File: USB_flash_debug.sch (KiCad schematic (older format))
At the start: 31 parts, among them IC2 TPS7A0518PDBVT, J6 E8124-015-01, J9 E8124-015-01, Q7 BSS138-7-F, Q8 BSS138-7-F, SW1 1X03, U13 FT232RQ-REEL, U9 FSUSB30MUX

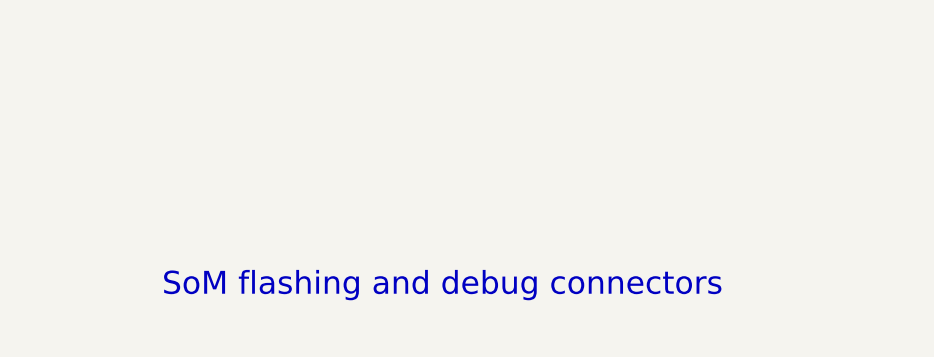
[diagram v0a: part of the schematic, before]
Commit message: Update the sch signage, remove redundant sheets
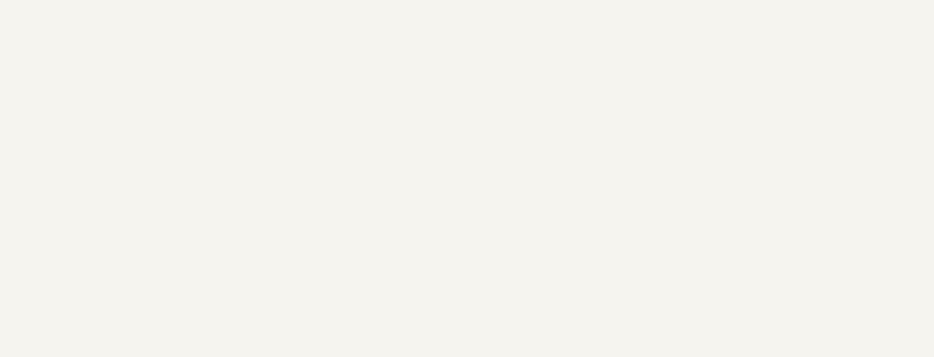
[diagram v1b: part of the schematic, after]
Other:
- note removed: "SoM flashing and debug connectors"

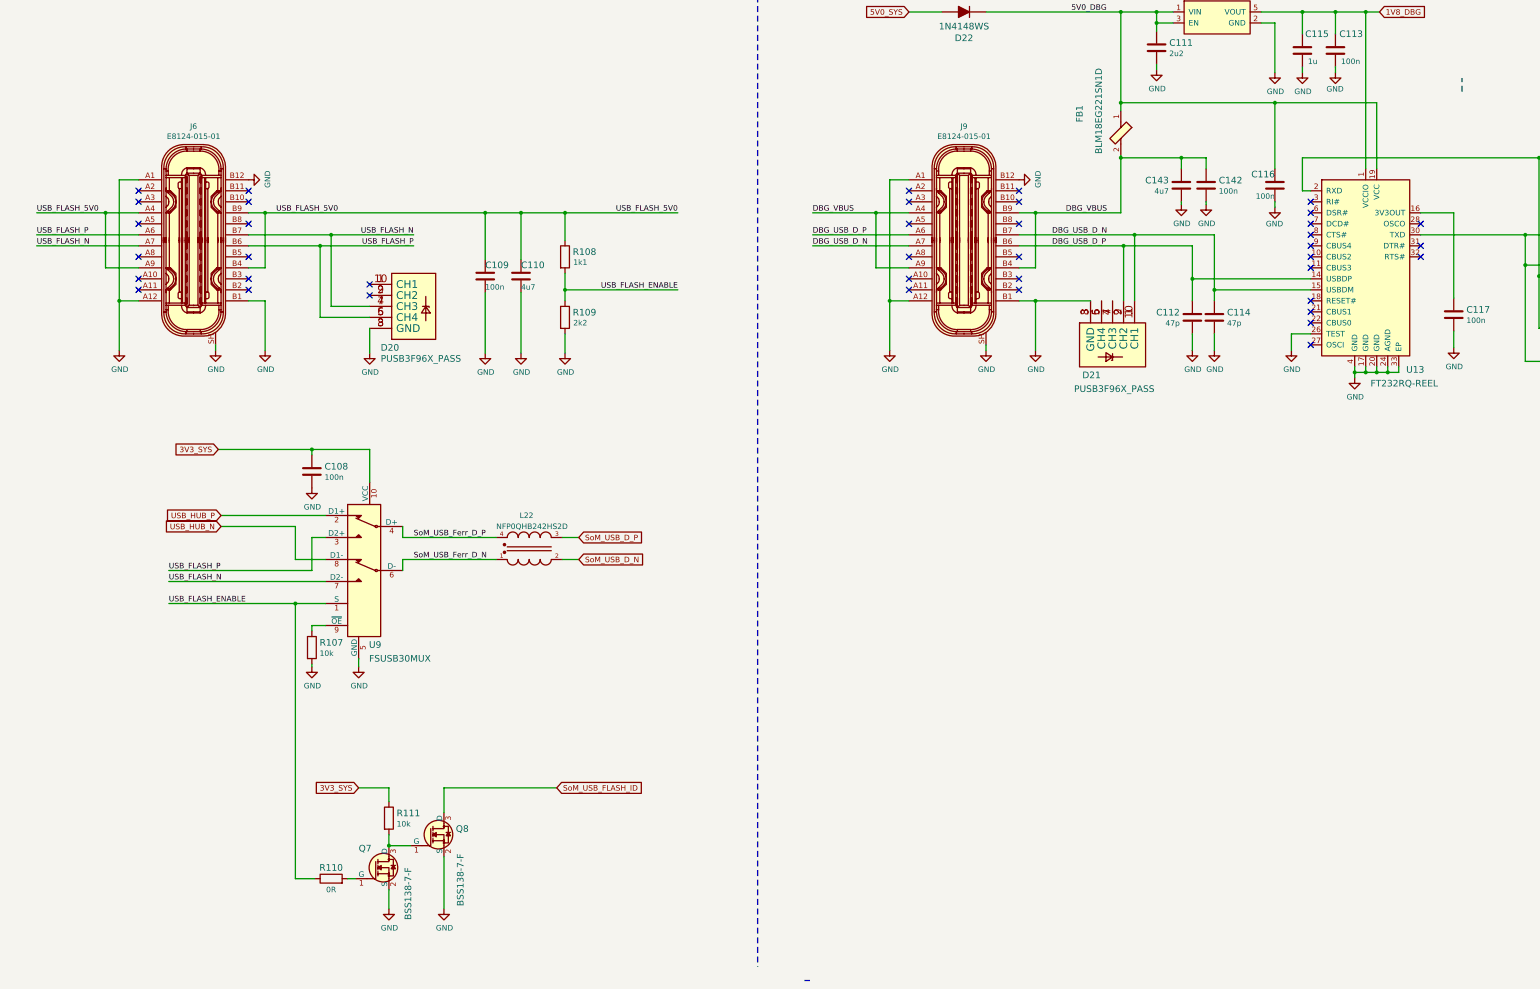
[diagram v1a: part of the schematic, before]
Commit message: Removed Q8, R111. SoM_USB_FLASH_ID changed from SoM's USB_ID to GPIO_1. Connected flash CC to SoM through 0R. Connected USB_VBUS to USB flash 5V via diode. SoM USB_ID connected to GPIO_1 through 0R
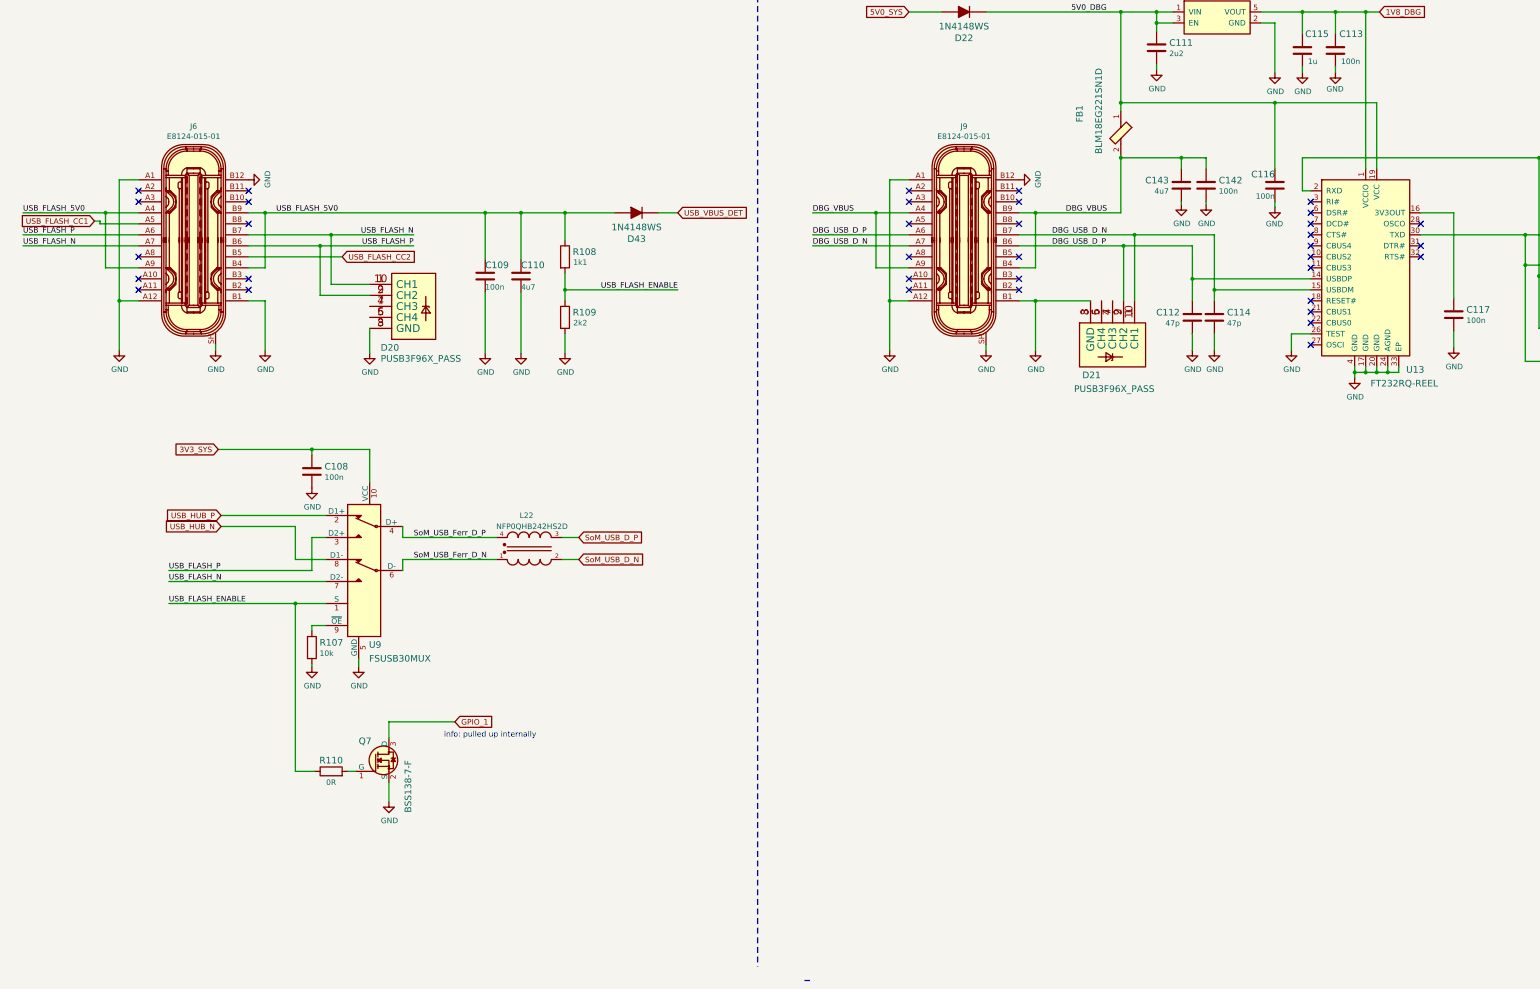
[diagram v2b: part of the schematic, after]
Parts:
- removed Q8: BSS138-7-F, sc606-baseboard-footprints:SOT-23-3, symbol sc606-baseboard:BSS138-7-F
- removed R111: R_10k_0402, sc606-baseboard-footprints:0402-res, symbol sc606-baseboard:R_10k_0402
- added D43: 1N4148WS, sc606-baseboard-footprints:SOD-323F, symbol sc606-baseboard:1N4148WS
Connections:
- net USB_FLASH_5V0: now also D43.A
- net USB_FLASH_N: now also D20.1 (CH1), D20.10 (CH1); no longer D20.4 (CH3), D20.7 (CH3)
- net USB_FLASH_P: now also D20.2 (CH2), D20.9 (CH2); no longer D20.5 (CH4), D20.6 (CH4)
- net USB_FLASH_CC1: now reaches J6.A5
- net USB_FLASH_CC2: now reaches J6.B5
- net GPIO_1: now reaches Q7.3 (D)
- new net: D20.4 (CH3), D20.7 (CH3)
- new net: D20.5 (CH4), D20.6 (CH4)
- new net USB_VBUS_DET: D43.K
- no-connect marks 40 -> 36
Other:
- note added: "info: pulled up internally"
- moved on the sheet: Q7, R110
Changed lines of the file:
@@
 	2925 3875 3575 3875
 Wire Wire Line
-	4025 4425 3675 4425
-Wire Wire Line
 	3675 3775 2925 3775
-Wire Wire Line
-	4025 4525 3575 4525
 $Comp
 L sc606-baseboard:GND #PWR0117
@@
 Connection ~ 3675 3775
 Wire Wire Line
-	3675 4425 3675 3775
-Wire Wire Line
-	3575 4525 3575 3875
-Wire Wire Line
 	3575 3875 4425 3875
 Wire Wire Line
@@
 L sc606-baseboard:GND #PWR0123
 U 1 1 62A39278
-P 4200 9900
-F 0 "#PWR0123" H 4200 9650 50  0001 C CNN
-F 1 "GND" H 4205 9727 50  0000 C CNN
-F 2 "" H 4200 9900 50  0001 C CNN
-F 3 "" H 4200 9900 50  0001 C CNN
-	1    4200 9900
+P 4200 8925
+F 0 "#PWR0123" H 4200 8675 50  0001 C CNN
+F 1 "GND" H 4205 8752 50  0000 C CNN
+F 2 "" H 4200 8925 50  0001 C CNN
+F 3 "" H 4200 8925 50  0001 C CNN
+	1    4200 8925
 	1    0    0    -1
 $EndComp
-Text GLabel 5725 8800 2    50   Input ~ 0
-SoM_USB_FLASH_ID
 $Comp
 L sc606-baseboard:R_0R_0402 R110
 U 1 1 62A4008D
-P 3675 9625
-F 0 "R110" H 3675 9725 60  0000 C CNN
-F 1 "R_0R_0402" H 3675 9475 60  0001 C CNN
-F 2 "sc606-baseboard-footprints:0402-res" H 3875 9825 60  0001 L CNN
-F 3 "" H 3675 9625 50  0001 C CNN
-F 4 "PANASONIC" H 3875 10025 60  0001 L CNN "Manufacturer"
-F 5 "ERJ2GE0R00X" H 3875 9925 60  0001 L CNN "MPN"
-F 6 "0R" H 3675 9525 50  0000 C CNN "Val"
-	1    3675 9625
+P 3675 8650
+F 0 "R110" H 3675 8750 60  0000 C CNN
+F 1 "R_0R_0402" H 3675 8500 60  0001 C CNN
+F 2 "sc606-baseboard-footprints:0402-res" H 3875 8850 60  0001 L CNN
+F 3 "" H 3675 8650 50  0001 C CNN
+F 4 "PANASONIC" H 3875 9050 60  0001 L CNN "Manufacturer"
+F 5 "ERJ2GE0R00X" H 3875 8950 60  0001 L CNN "MPN"
+F 6 "0R" H 3675 8550 50  0000 C CNN "Val"
+	1    3675 8650
 	1    0    0    -1
 $EndComp
@@
 L sc606-baseboard:BSS138-7-F Q7
 U 1 1 62A49D1F
-P 4200 9525
-F 0 "Q7" H 3925 9700 60  0000 L CNN
-F 1 "BSS138-7-F" V 4375 9050 60  0000 L CNN
-F 2 "sc606-baseboard-footprints:SOT-23-3" H 4400 9725 60  0001 L CNN
-F 3 "https://www.diodes.com/assets/Datasheets/ds30144.pdf" H 4400 9825 60  0001 L CNN
-F 4 "BSS138-7-F" H 4400 10025 60  0001 L CNN "MPN"
-F 5 "Diodes Incorporated" H 4400 10625 60  0001 L CNN "Manufacturer"
-	1    4200 9525
+P 4200 8550
+F 0 "Q7" H 3925 8725 60  0000 L CNN
+F 1 "BSS138-7-F" V 4375 8075 60  0000 L CNN
+F 2 "sc606-baseboard-footprints:SOT-23-3" H 4400 8750 60  0001 L CNN
+F 3 "https://www.diodes.com/assets/Datasheets/ds30144.pdf" H 4400 8850 60  0001 L CNN
+F 4 "BSS138-7-F" H 4400 9050 60  0001 L CNN "MPN"
+F 5 "Diodes Incorporated" H 4400 9650 60  0001 L CNN "Manufacturer"
+	1    4200 8550
 	1    0    0    -1
 $EndComp
 $Comp
-L sc606-baseboard:BSS138-7-F Q8
-U 1 1 62A4B7F6
-P 4700 9225
-F 0 "Q8" H 4808 9278 60  0000 L CNN
-F 1 "BSS138-7-F" V 4850 8575 60  0000 L CNN
-F 2 "sc606-baseboard-footprints:SOT-23-3" H 4900 9425 60  0001 L CNN
-F 3 "https://www.diodes.com/assets/Datasheets/ds30144.pdf" H 4900 9525 60  0001 L CNN
-F 4 "BSS138-7-F" H 4900 9725 60  0001 L CNN "MPN"
-F 5 "Diodes Incorporated" H 4900 10325 60  0001 L CNN "Manufacturer"
-	1    4700 9225
-	1    0    0    -1
-$EndComp
-Wire Wire Line
-	4400 9325 4200 9325
-Wire Wire Line
-	4700 8800 4700 9025
-Wire Wire Line
-	4700 8800 5725 8800
-Text GLabel 3925 8800 0    50   Input ~ 0
-3V3_SYS
-$Comp
-L sc606-baseboard:R_10k_0402 R111
-U 1 1 62A4EC7F
-P 4200 9075
-F 0 "R111" V 4155 9145 60  0000 L CNN
-F 1 "R_10k_0402" H 4200 8925 60  0001 C CNN
-F 2 "sc606-baseboard-footprints:0402-res" H 4400 9275 60  0001 L CNN
-F 3 "" H 4200 9075 50  0001 C CNN
-F 4 "VISHAY" H 4400 9475 60  0001 L CNN "Manufacturer"
-F 5 "CRCW040210K0FKEDHP" H 4400 9375 60  0001 L CNN "MPN"
-F 6 "10k" V 4253 9145 50  0000 L CNN "Val"
-	1    4200 9075
-	0    1    1    0
-$EndComp
-Wire Wire Line
-	4200 9225 4200 9325
-Connection ~ 4200 9325
-$Comp
 L sc606-baseboard:1X03 SW1
 U 1 1 63004CC0
@@
 Text Label 3175 3575 0    50   ~ 0
 USB_FLASH_5V0
-Text Label 6825 3575 2    50   ~ 0
-USB_FLASH_5V0
 Text Label 10400 1750 0    50   ~ 0
 5V0_DBG
@@
 $EndComp
 Wire Wire Line
-	6825 3575 5800 3575
+	6825 3575 6650 3575
 $Comp
 L sc606-baseboard:GND #PWR0167
@@
 	0    -1   -1   0
 $EndComp
-Text Label 1000 3575 0    50   ~ 0
+Text Label 875  3575 0    50   ~ 0
 USB_FLASH_5V0
 Wire Wire Line
-	1000 3575 1625 3575
-NoConn ~ 4025 4225
-NoConn ~ 4025 4325
+	875  3575 1625 3575
 NoConn ~ 2925 3375
 NoConn ~ 2925 3475
 NoConn ~ 2925 3675
-NoConn ~ 2925 3975
 NoConn ~ 2925 4175
 NoConn ~ 2925 4275
@@
 NoConn ~ 1925 4175
 NoConn ~ 1925 3975
-NoConn ~ 1925 3675
 NoConn ~ 1925 3475
 NoConn ~ 1925 3375
 Wire Wire Line
-	1925 3775 1000 3775
+	1925 3775 875  3775
 Wire Wire Line
-	1000 3875 1925 3875
-Text Label 1000 3775 0    50   ~ 0
+	875  3875 1925 3875
+Text Label 875  3775 0    50   ~ 0
 USB_FLASH_P
-Text Label 1000 3875 0    50   ~ 0
+Text Label 875  3875 0    50   ~ 0
 USB_FLASH_N
 $Comp
@@
 	3500 5725 4025 5725
 Wire Wire Line
-	4200 8925 4200 8800
+	4200 8750 4200 8925
 Wire Wire Line
-	4200 8800 3925 8800
-$Comp
-L sc606-baseboard:GND #PWR050
-U 1 1 625B110A
-P 4700 9900
-F 0 "#PWR050" H 4700 9650 50  0001 C CNN
-F 1 "GND" H 4705 9727 50  0000 C CNN
-F 2 "" H 4700 9900 50  0001 C CNN
-F 3 "" H 4700 9900 50  0001 C CNN
-	1    4700 9900
-	1    0    0    -1
-$EndComp
+	3900 8650 3825 8650
 Wire Wire Line
-	4200 9725 4200 9900
+	3525 8650 3350 8650
 Wire Wire Line
-	4700 9425 4700 9900
-Wire Wire Line
-	3900 9625 3825 9625
-Wire Wire Line
-	3525 9625 3350 9625
-Wire Wire Line
-	3350 9625 3350 7125
+	3350 8650 3350 7125
 Connection ~ 3350 7125
 Wire Wire Line
@@
 	1    0    0    -1
 $EndComp
-Wire Notes Line
-	13950 2475 13950 2350
 Wire Wire Line
 	11175 2275 11175 2225
@@
 EndData
 $EndBitmap
+Text GLabel 6825 3575 2    50   Input ~ 0
+USB_VBUS_DET
+$Comp
+L sc606-baseboard:1N4148WS D43
+U 1 1 6293E44B
+P 6450 3575
+F 0 "D43" H 6450 3338 60  0000 C CNN
+F 1 "1N4148WS" H 6450 3444 60  0000 C CNN
+F 2 "sc606-baseboard-footprints:SOD-323F" H 6650 3775 60  0001 L CNN
+F 3 "https://www.onsemi.com/pub/Collateral/1N914BWS-D.pdf" H 6650 3875 60  0001 L CNN
+F 4 "1N4148WS" H 6650 4075 60  0001 L CNN "MPN"
+F 5 "ON Semiconductor" H 6650 4675 60  0001 L CNN "Manufacturer"
+	1    6450 3575
+	1    0    0    -1
+$EndComp
+Wire Wire Line
+	6250 3575 5800 3575
+Wire Wire Line
+	4200 8350 4200 8200
+Wire Wire Line
+	4200 8200 4800 8200
+Text Notes 4700 8350 0    50   ~ 0
+info: pulled up internally
+Wire Wire Line
+	1575 3675 1925 3675
+Text GLabel 4800 8200 2    50   Input ~ 0
+GPIO_1
+Text GLabel 1525 3650 0    50   Input ~ 0
+USB_FLASH_CC1
+Text GLabel 3775 3975 2    50   Input ~ 0
+USB_FLASH_CC2
+Wire Wire Line
+	2925 3975 3775 3975
+Wire Wire Line
+	1575 3675 1575 3650
+Wire Wire Line
+	1575 3650 1525 3650
+Wire Wire Line
+	4025 4225 3675 4225
+Wire Wire Line
+	3675 4225 3675 3775
+Wire Wire Line
+	4025 4325 3575 4325
+Wire Wire Line
+	3575 4325 3575 3875
 $EndSCHEMATC
